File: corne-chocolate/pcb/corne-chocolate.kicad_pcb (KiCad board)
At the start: 2 copper layers, 133.8 x 91.4 mm, 98 parts, among them J3 LED, P1 i2c-pin, P2 i2c-pin, SW1 SW_PUSH, SW10 SW_PUSH, SW11 SW_PUSH, SW12 SW_PUSH, SW13 SW_PUSH, SW14 SW_PUSH, SW15 SW_PUSH, SW16 SW_PUSH, SW17 SW_PUSH, SW18 SW_PUSH, SW19 SW_PUSH, SW2 SW_PUSH, SW20 SW_PUSH, SW21 SW_PUSH, SW3 SW_PUSH, SW4 SW_PUSH, SW5 SW_PUSH, SW6 SW_PUSH, SW7 SW_PUSH, SW8 SW_PUSH, SW9 SW_PUSH, U1 ProMicro

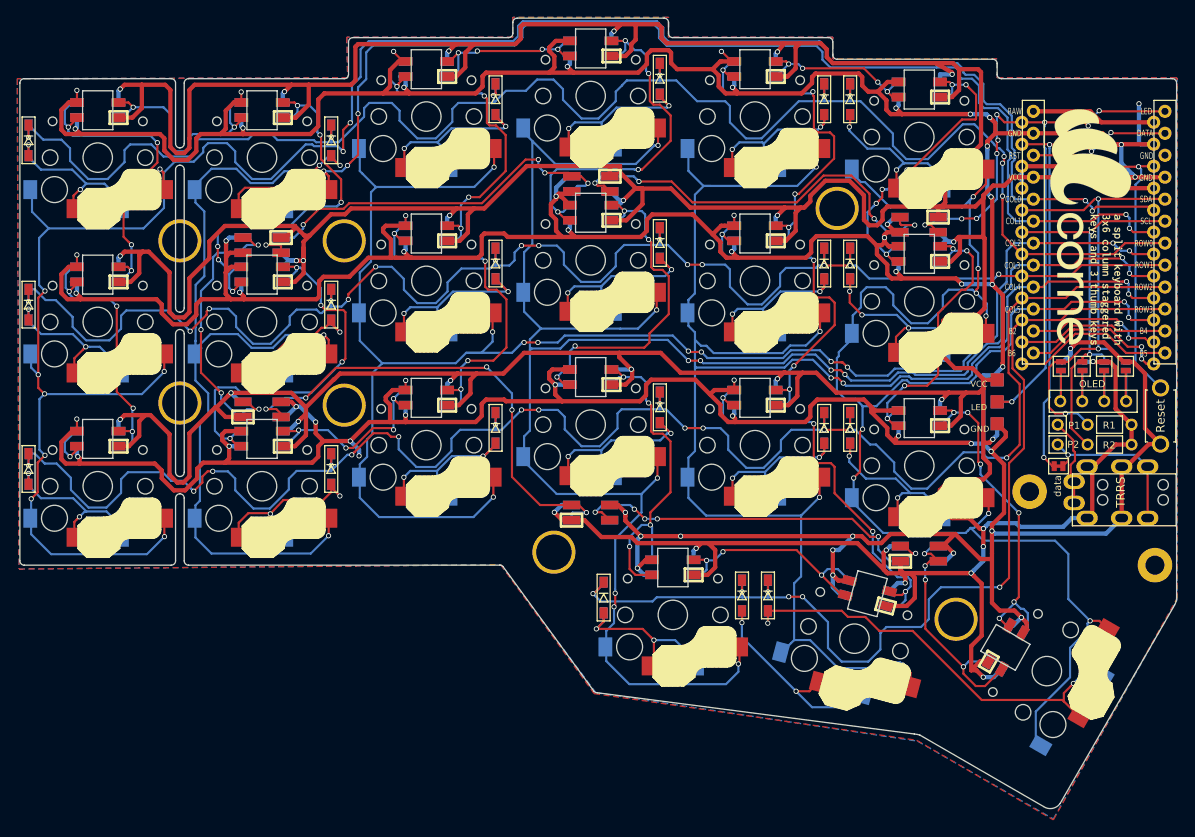
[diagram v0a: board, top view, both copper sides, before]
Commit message: cleanup symbol library. copy symbols from pcb to new project specific library
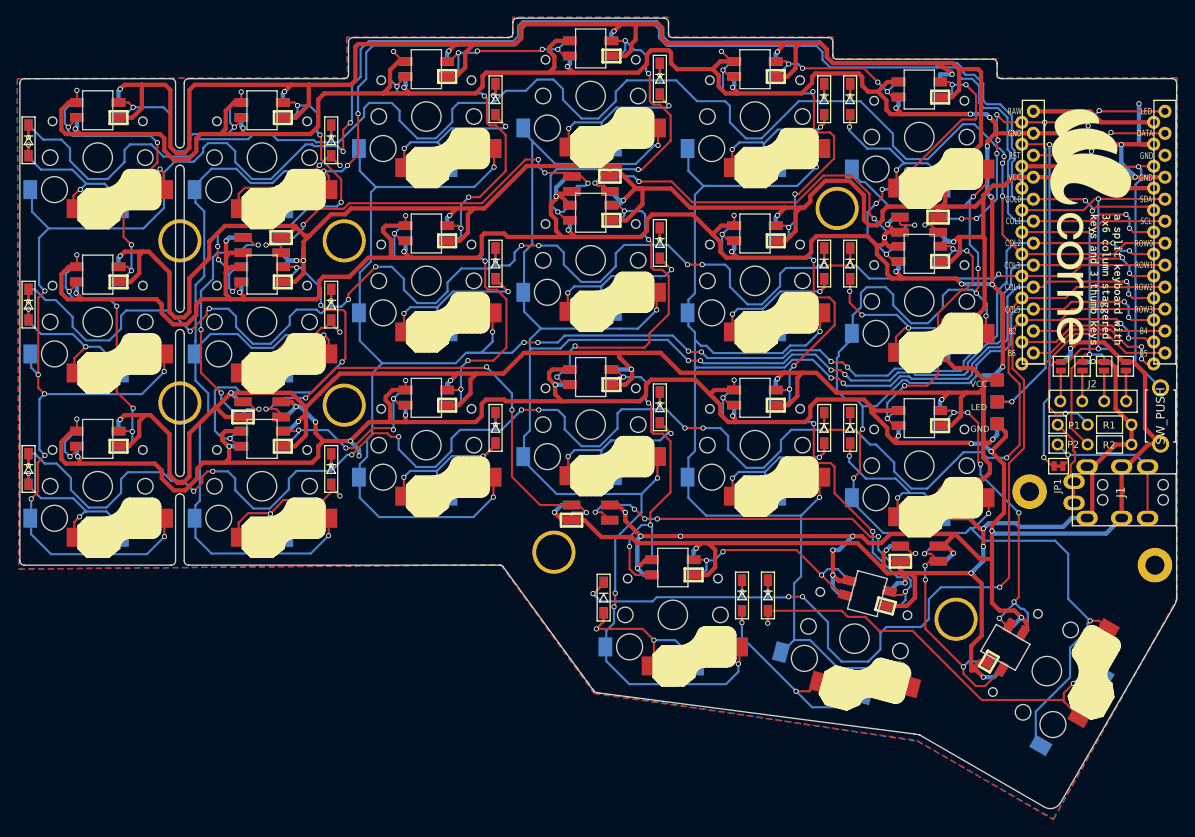
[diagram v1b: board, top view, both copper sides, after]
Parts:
- D1, D10, D11, D12, D13, D14, D15, D16, D17, D18, D19, D2, D20, D21, D3, D4, D5, D6, D7, D8, D9: footprint kbd:D3_SMD -> corne-chocolate:D3_SMD
- RSW1: value Reset -> SW_PUSH
- SW1, SW10, SW11, SW12, SW13, SW14, SW15, SW16, SW17, SW18, SW19, SW2, SW20, SW3, SW4, SW5, SW6, SW7, SW8, SW9: footprint kbd:Choc_Hotswap -> corne-chocolate:Choc_Hotswap
- SW21: footprint kbd:Choc_Hotswap_1.5u -> corne-chocolate:Choc_Hotswap_1.5u
- renumbered TRRS to J1, OLED to J2, data to JP1
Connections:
- D1 pad 2: Net-(D1-Pad2) -> (no net)
- D10 pad 2: Net-(D10-Pad2) -> (no net)
- D11 pad 2: Net-(D11-Pad2) -> (no net)
- D12 pad 2: Net-(D12-Pad2) -> (no net)
- D13 pad 2: Net-(D13-Pad2) -> (no net)
- D14 pad 2: Net-(D14-Pad2) -> (no net)
- D15 pad 2: Net-(D15-Pad2) -> (no net)
- D16 pad 2: Net-(D16-Pad2) -> (no net)
- D17 pad 2: Net-(D17-Pad2) -> (no net)
- D18 pad 2: Net-(D18-Pad2) -> (no net)
- D19 pad 2: Net-(D19-Pad2) -> (no net)
- D2 pad 2: Net-(D2-Pad2) -> (no net)
- D20 pad 2: Net-(D20-Pad2) -> (no net)
- D21 pad 2: Net-(D21-Pad2) -> (no net)
- D3 pad 2: Net-(D3-Pad2) -> (no net)
- D4 pad 2: Net-(D4-Pad2) -> (no net)
- D5 pad 2: Net-(D5-Pad2) -> (no net)
- D6 pad 2: Net-(D6-Pad2) -> (no net)
- D7 pad 2: Net-(D7-Pad2) -> (no net)
- D8 pad 2: Net-(D8-Pad2) -> (no net)
- D9 pad 2: Net-(D9-Pad2) -> (no net)
- J1 pad A: Net-(J1-PadA) -> (no net)
- J1 pad B: Net-(J1-PadB) -> (no net)
- J2 pad 1: Net-(J2-Pad1) -> (no net)
- J2 pad 2: Net-(J2-Pad2) -> (no net)
- J2 pad 3: Net-(J2-Pad3) -> (no net)
- J2 pad 4: Net-(J2-Pad4) -> (no net)
- JP1 pad 2: Net-(J1-PadB) -> Net-(P2-Pin_1)
- JP2 pad 2: Net-(J2-Pad4) -> Net-(J2-Pin_4)
- JP3 pad 2: Net-(J2-Pad3) -> Net-(J2-Pin_3)
- JP4 pad 2: Net-(J2-Pad2) -> Net-(J2-Pin_2)
- JP5 pad 2: Net-(J2-Pad1) -> Net-(J2-Pin_1)
- JP6 pad 2: Net-(J2-Pad4) -> Net-(J2-Pin_4)
- JP7 pad 2: Net-(J2-Pad3) -> Net-(J2-Pin_3)
- JP8 pad 2: Net-(J2-Pad2) -> Net-(J2-Pin_2)
- JP9 pad 2: Net-(J2-Pad1) -> Net-(J2-Pin_1)
- L1 pad 1: Net-(L1-Pad1) -> (no net)
- L1 pad 3: Net-(L1-Pad3) -> (no net)
- L10 pad 1: Net-(L10-Pad1) -> Net-(L10-DOUT)
- L10 pad 3: Net-(L10-Pad3) -> (no net)
- L11 pad 1: Net-(L11-Pad1) -> (no net)
- L11 pad 3: Net-(L11-Pad3) -> Net-(L11-DIN)
- L12 pad 1: Net-(L12-Pad1) -> Net-(L12-DOUT)
- L12 pad 3: Net-(L12-Pad3) -> (no net)
- L13 pad 1: Net-(L13-Pad1) -> (no net)
- L13 pad 3: Net-(L13-Pad3) -> Net-(L13-DIN)
- L14 pad 1: Net-(L14-Pad1) -> Net-(L14-DOUT)
- L14 pad 3: Net-(L14-Pad3) -> (no net)
- L15 pad 1: Net-(L14-Pad3) -> Net-(L14-DIN)
- L15 pad 3: Net-(L15-Pad3) -> Net-(L15-DIN)
- L16 pad 1: Net-(L10-Pad3) -> Net-(L10-DIN)
- L16 pad 3: Net-(L16-Pad3) -> (no net)
- L17 pad 1: Net-(L17-Pad1) -> (no net)
- L17 pad 3: Net-(L11-Pad1) -> Net-(L11-DOUT)
- L18 pad 1: Net-(L12-Pad3) -> Net-(L12-DIN)
- L18 pad 3: Net-(L18-Pad3) -> (no net)
- L19 pad 1: Net-(L16-Pad3) -> Net-(L16-DIN)
- L19 pad 3: Net-(L19-Pad3) -> (no net)
- L2 pad 1: Net-(L1-Pad3) -> Net-(L1-DIN)
- L2 pad 3: Net-(L2-Pad3) -> (no net)
- L20 pad 1: Net-(L19-Pad3) -> Net-(L19-DIN)
- L20 pad 3: Net-(L17-Pad1) -> Net-(L17-DOUT)
- L21 pad 1: Net-(L18-Pad3) -> Net-(L18-DIN)
- L21 pad 3: Net-(L21-Pad3) -> (no net)
- L22 pad 1: Net-(L22-Pad1) -> (no net)
- L22 pad 3: Net-(L22-Pad3) -> (no net)
- L23 pad 1: Net-(L22-Pad3) -> Net-(L22-DIN)
- L23 pad 3: Net-(L23-Pad3) -> (no net)
- L24 pad 1: Net-(L23-Pad3) -> Net-(L23-DIN)
- L25 pad 1: Net-(L25-Pad1) -> (no net)
- L25 pad 3: Net-(L22-Pad1) -> Net-(L22-DOUT)
- L26 pad 1: Net-(L26-Pad1) -> (no net)
- L26 pad 3: Net-(L25-Pad1) -> Net-(L25-DOUT)
- L27 pad 1: Net-(L21-Pad3) -> Net-(L21-DIN)
- L27 pad 3: Net-(L26-Pad1) -> Net-(L26-DOUT)
- L3 pad 1: Net-(L3-Pad1) -> (no net)
- L3 pad 3: Net-(L3-Pad3) -> (no net)
- L4 pad 1: Net-(L3-Pad3) -> Net-(L3-DIN)
- L4 pad 3: Net-(L10-Pad1) -> (no net)
- L5 pad 1: Net-(L11-Pad3) -> (no net)
- L5 pad 3: Net-(L5-Pad3) -> (no net)
- L6 pad 1: Net-(L5-Pad3) -> Net-(L5-DIN)
- L6 pad 3: Net-(L12-Pad1) -> (no net)
- L7 pad 1: Net-(L13-Pad3) -> (no net)
- L7 pad 3: Net-(L1-Pad1) -> Net-(L1-DOUT)
- L8 pad 1: Net-(L2-Pad3) -> Net-(L2-DIN)
- L8 pad 3: Net-(L14-Pad1) -> (no net)
- L9 pad 1: Net-(L15-Pad3) -> (no net)
- L9 pad 3: Net-(L3-Pad1) -> Net-(L3-DOUT)
- P1 pad 1: Net-(J1-PadA) -> Net-(P1-Pin_1)
- P2 pad 1: Net-(J1-PadB) -> Net-(P2-Pin_1)
- SW1 pad 2: Net-(D1-Pad2) -> Net-(D1-A)
- SW10 pad 2: Net-(D10-Pad2) -> Net-(D10-A)
- SW11 pad 2: Net-(D11-Pad2) -> Net-(D11-A)
- SW12 pad 2: Net-(D12-Pad2) -> Net-(D12-A)
- SW13 pad 2: Net-(D13-Pad2) -> Net-(D13-A)
- SW14 pad 2: Net-(D14-Pad2) -> Net-(D14-A)
- SW15 pad 2: Net-(D15-Pad2) -> Net-(D15-A)
- SW16 pad 2: Net-(D16-Pad2) -> Net-(D16-A)
- SW17 pad 2: Net-(D17-Pad2) -> Net-(D17-A)
- SW18 pad 2: Net-(D18-Pad2) -> Net-(D18-A)
- SW19 pad 2: Net-(D19-Pad2) -> Net-(D19-A)
- SW2 pad 2: Net-(D2-Pad2) -> Net-(D2-A)
- SW20 pad 2: Net-(D20-Pad2) -> Net-(D20-A)
- SW21 pad 2: Net-(D21-Pad2) -> Net-(D21-A)
- SW3 pad 2: Net-(D3-Pad2) -> Net-(D3-A)
- SW4 pad 2: Net-(D4-Pad2) -> Net-(D4-A)
- SW5 pad 2: Net-(D5-Pad2) -> Net-(D5-A)
- SW6 pad 2: Net-(D6-Pad2) -> Net-(D6-A)
- SW7 pad 2: Net-(D7-Pad2) -> Net-(D7-A)
- SW8 pad 2: Net-(D8-Pad2) -> Net-(D8-A)
- SW9 pad 2: Net-(D9-Pad2) -> Net-(D9-A)
- U1 pad 11: Net-(U1-Pad11) -> (no net)
- U1 pad 12: Net-(U1-Pad12) -> (no net)
- U1 pad 13: Net-(U1-Pad13) -> (no net)
- U1 pad 14: Net-(U1-Pad14) -> (no net)
- U1 pad 24: Net-(U1-Pad24) -> (no net)
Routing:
- net Net-(L25-Pad1): track 56.6 -> 0.00 mm, vias 5 -> 0
- net Net-(L25-DOUT): track 0.00 -> 56.6 mm, vias 0 -> 5
- net Net-(D21-Pad2): track 50.2 -> 0.00 mm, vias 2 -> 0
- net Net-(D21-A): track 0.00 -> 50.2 mm, vias 0 -> 2
- net Net-(L23-Pad3): track 48.9 -> 0.00 mm, vias 4 -> 0
- net Net-(L23-DIN): track 0.00 -> 48.9 mm, vias 0 -> 4
- net Net-(L22-Pad3): track 48.6 -> 0.00 mm, vias 5 -> 0
- net Net-(L22-DIN): track 0.00 -> 48.6 mm, vias 0 -> 5
- net Net-(L17-Pad1): track 48.0 -> 0.00 mm, vias 4 -> 0
- net Net-(L17-DOUT): track 0.00 -> 48.0 mm, vias 0 -> 4
- net Net-(L2-Pad3): track 46.2 -> 0.00 mm, vias 6 -> 0
- net Net-(L2-DIN): track 0.00 -> 46.2 mm, vias 0 -> 6
- net Net-(L14-Pad1): track 45.6 -> 0.00 mm, vias 4 -> 0
- net Net-(L14-DOUT): track 0.00 -> 45.6 mm, vias 0 -> 4
- net Net-(L26-Pad1): track 45.5 -> 0.00 mm, vias 6 -> 0
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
